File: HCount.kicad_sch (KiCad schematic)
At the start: 10 parts, among them U2 74HC11, U3 74HC163, U4 74HC163, U5 74HC163, U6 74HC688

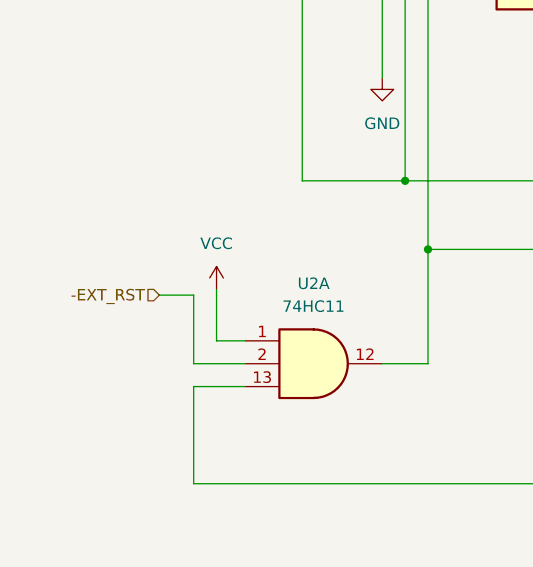
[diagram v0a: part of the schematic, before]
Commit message: allow hcount reset when frame ends
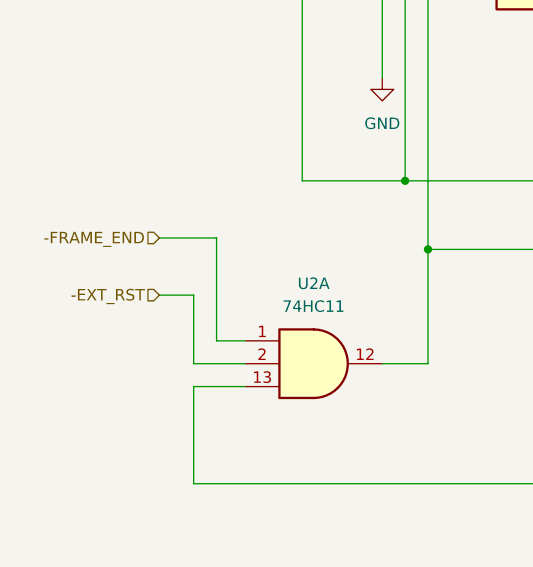
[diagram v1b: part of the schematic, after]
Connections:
- net VCC: no longer U2.1
- new net -FRAME_END: U2.1
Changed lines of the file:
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@@
+    (stroke (width 0) (type default))
+  )
+  (wire (pts (xy 27.305 126.365) (xy 33.655 126.365))
     (stroke (width 0) (type default))
   )
@@
     (stroke (width 0) (type default))
   )
-  (wire (pts (xy 33.655 132.08) (xy 33.655 137.795))
+  (wire (pts (xy 33.655 126.365) (xy 33.655 137.795))
     (stroke (width 0) (type default))
   )
@@
   (hierarchical_label "HC0" (shape output) (at 218.44 17.78 0) (fields_autoplaced)
     (effects (font (size 1.27 1.27)) (justify left))
+  )
+  (hierarchical_label "-FRAME_END" (shape input) (at 27.305 126.365 180) (fields_autoplaced)
+    (effects (font (size 1.27 1.27)) (justify right))
   )
   (hierarchical_label "HC1" (shape output) (at 218.44 20.32 0) (fields_autoplaced)
@@
         )
       )
-    )
-  )
-  (symbol (lib_id "power:VCC") (at 33.655 132.08 0) (unit 1)
-    (in_bom yes) (on_board yes) (dnp no) (fields_autoplaced)
-    (property "Reference" "#PWR03" (at 33.655 135.89 0)
-      (effects (font (size 1.27 1.27)) hide)
-    )
-    (property "Value" "VCC" (at 33.655 127 0)
-      (effects (font (size 1.27 1.27)))
-    )
-    (property "Footprint" "" (at 33.655 132.08 0)
-      (effects (font (size 1.27 1.27)) hide)
-    )
-    (property "Datasheet" "" (at 33.655 132.08 0)
-      (effects (font (size 1.27 1.27)) hide)
-    )
-    (pin "1")
-    (instances
-      (project "HW_VGA"
-        (path "/c4bd4b39-993a-4195-805f-b4de6fa4aea5/0f1cb3c4-c993-4160-bf3e-944843924f41"
-          (reference "#PWR03") (unit 1)
-        )
-      )

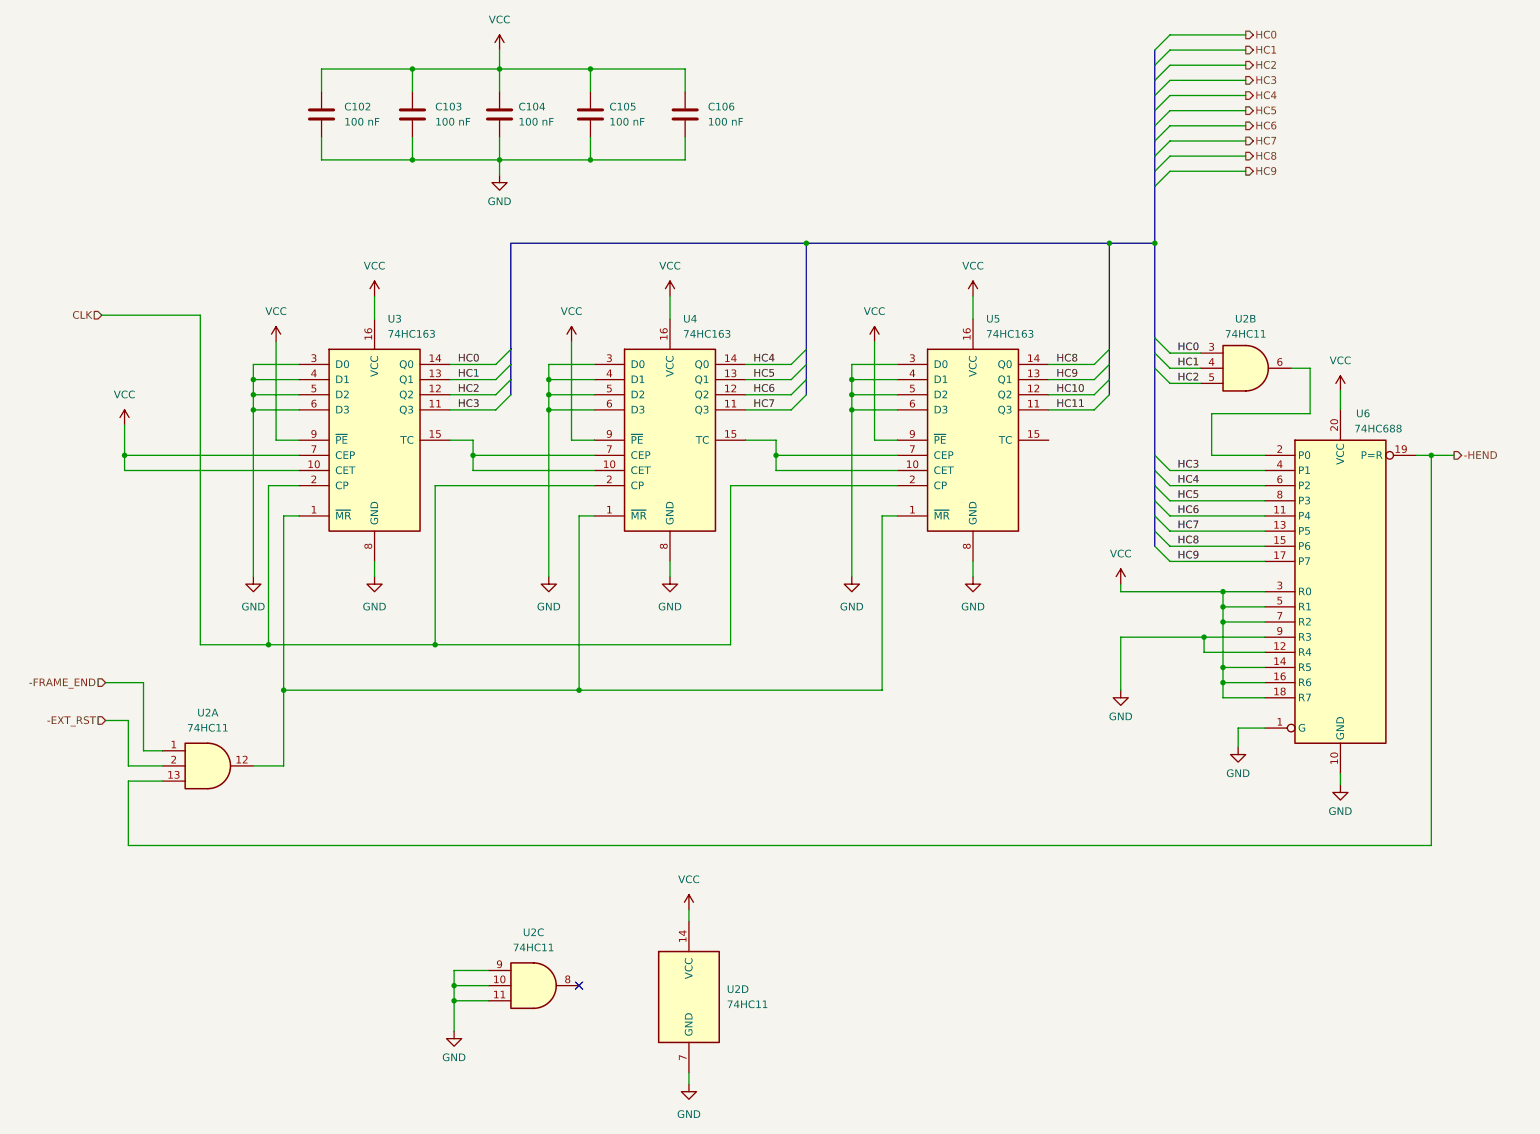
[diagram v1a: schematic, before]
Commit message: replace horizontal count logic with GAL22V10
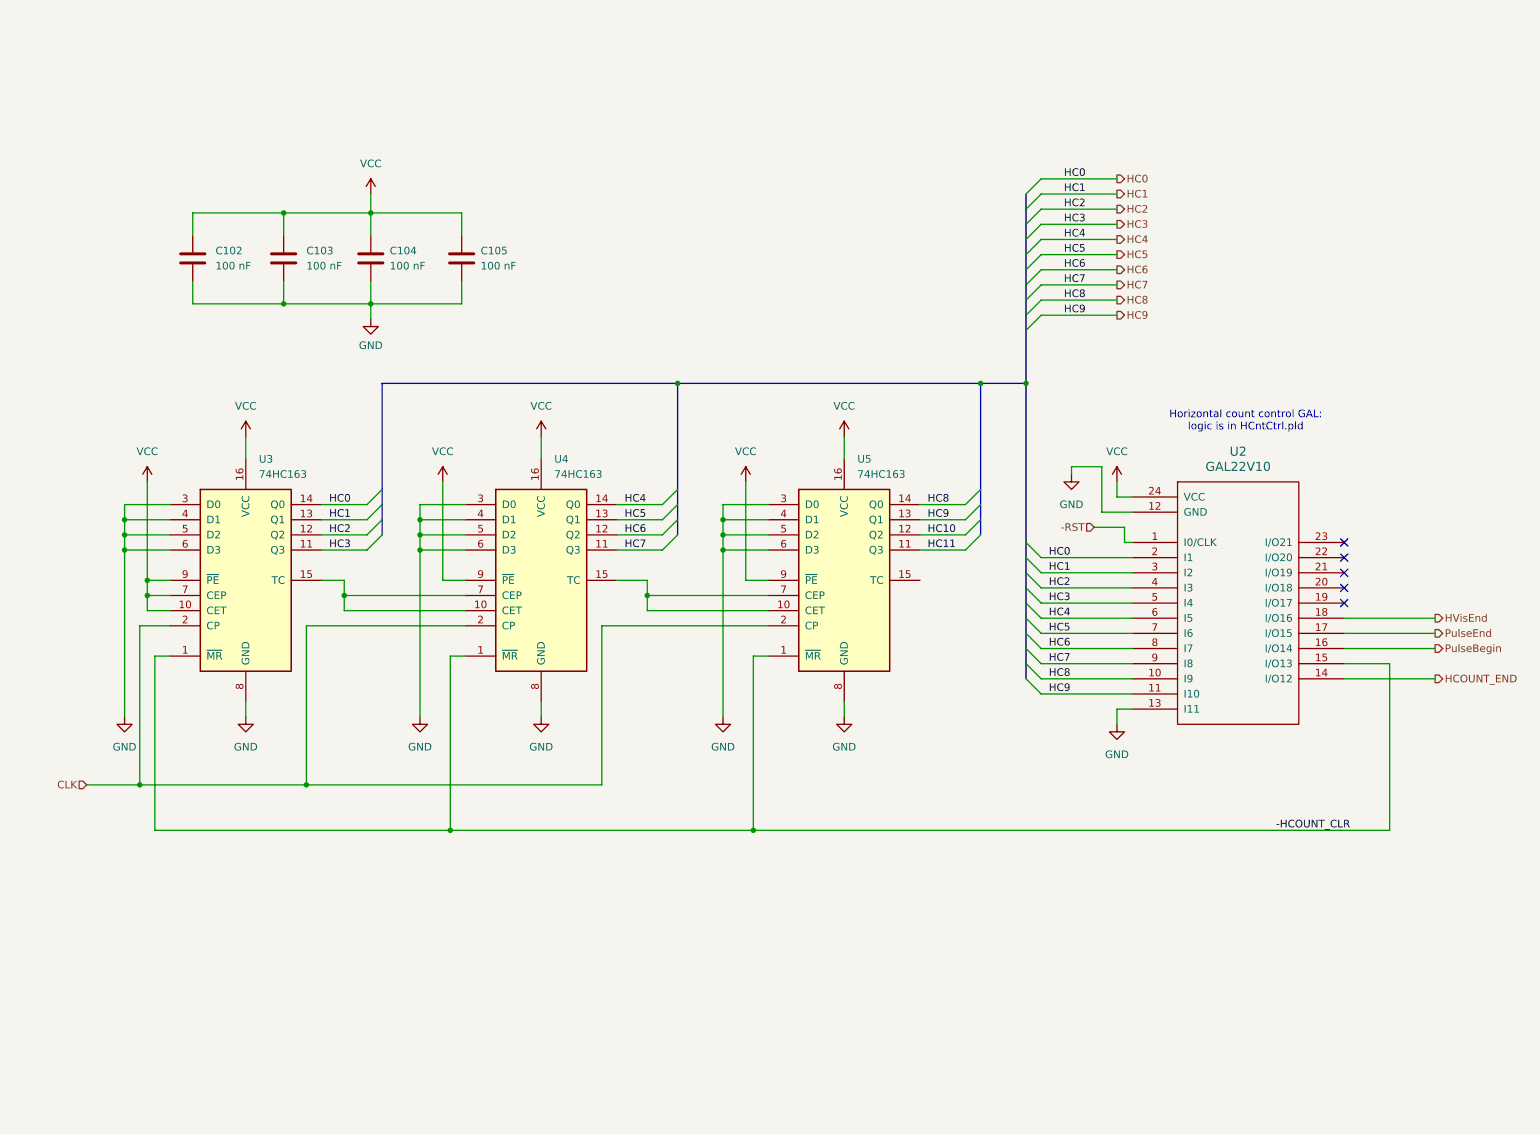
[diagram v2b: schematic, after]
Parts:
- removed C106: 100 nF, symbol Device:C
- removed U2: 74HC11, symbol 74xx:74LS11
- removed U6: 74HC688, symbol 74xx:74LS688
- added U2: GAL22V10, symbol ya68k:GAL22V10
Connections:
- net GND: now also U2.12 (GND), U2.13 (I11)
- net HC0: now also U2.2 (I1)
- net HC1: now also U2.3 (I2)
- net HC2: now also U2.4 (I3)
- net HC3: now also U2.5 (I4)
- net HC4: now also U2.6 (I5)
- net HC5: now also U2.7 (I6)
- net HC6: now also U2.8 (I7)
- net HC7: now also U2.9 (I8)
- net HC8: now also U2.10 (I9)
- net HC9: now also U2.11 (I10)
- net VCC: now also U2.24 (VCC)
- net -HCOUNT_CLR: now reaches U3.1 (~{MR}), U4.1 (~{MR}), U5.1 (~{MR})
- net -HCOUNT_CLR: now also U2.15 (I/O13)
- new net -RST: U2.1 (I0/CLK)
- new net HCOUNT_END: U2.14 (I/O12)
- new net HVisEnd: U2.18 (I/O16)
- new net PulseBegin: U2.16 (I/O14)
- new net PulseEnd: U2.17 (I/O15)
- no-connect marks 1 -> 5
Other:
- note added: "Horizontal count control GAL: logic is in HCntCtrl.pld"
- moved on the sheet: C102, C103, C104, C105, U3, U4, U5

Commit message: start working on VCount module
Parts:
- renumbered U2 to U102, U3 to U103, U4 to U104, U5 to U105
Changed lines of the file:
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@@
 		(dnp no)
 		(fields_autoplaced yes)
-		(property "Reference" "U3"
+		(property "Reference" "U103"
 			(at 52.9941 88.9 0)
 			(effects
@@
 			(project "HW_VGA"
 				(path "/c4bd4b39-993a-4195-805f-b4de6fa4aea5/0f1cb3c4-c993-4160-bf3e-944843924f41"
-					(reference "U3")
+					(reference "U103")
 					(unit 1)
 				)
@@
 		(dnp no)
 		(fields_autoplaced yes)
-		(property "Reference" "U2"
+		(property "Reference" "U102"
 			(at 217.17 87.63 0)
 			(effects
@@
 			(project "HW_VGA"
 				(path "/c4bd4b39-993a-4195-805f-b4de6fa4aea5/0f1cb3c4-c993-4160-bf3e-944843924f41"
-					(reference "U2")
+					(reference "U102")
 					(unit 1)
 				)
@@
 		(dnp no)
 		(fields_autoplaced yes)
-		(property "Reference" "U5"
+		(property "Reference" "U105"
 			(at 153.3241 88.9 0)
 			(effects
@@
 			(project "HW_VGA"
 				(path "/c4bd4b39-993a-4195-805f-b4de6fa4aea5/0f1cb3c4-c993-4160-bf3e-944843924f41"
-					(reference "U5")
+					(reference "U105")
 					(unit 1)
 				)
@@
 		(dnp no)
 		(fields_autoplaced yes)
-		(property "Reference" "U4"
+		(property "Reference" "U104"
 			(at 102.5241 88.9 0)
 			(effects
@@
 			(project "HW_VGA"
 				(path "/c4bd4b39-993a-4195-805f-b4de6fa4aea5/0f1cb3c4-c993-4160-bf3e-944843924f41"
-					(reference "U4")
-					(unit 1)
-				)
+					(reference "U104")
+					(unit 1)
+				)

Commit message: chips driven by GAL or memory need to be 74HCT
I forgot that GALs only guarantee 2.4V as the minimum
output high voltage. Bleh.
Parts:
- U103, U104, U105: value 74HC163 -> 74HCT163
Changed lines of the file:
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@@
 			)
 		)
-		(property "Value" "74HC163"
+		(property "Value" "74HCT163"
 			(at 52.9941 91.44 0)
 			(effects
@@
 			)
 		)
-		(property "Value" "74HC163"
+		(property "Value" "74HCT163"
 			(at 153.3241 91.44 0)
 			(effects
@@
 			)
 		)
-		(property "Value" "74HC163"
+		(property "Value" "74HCT163"
 			(at 102.5241 91.44 0)
 			(effects

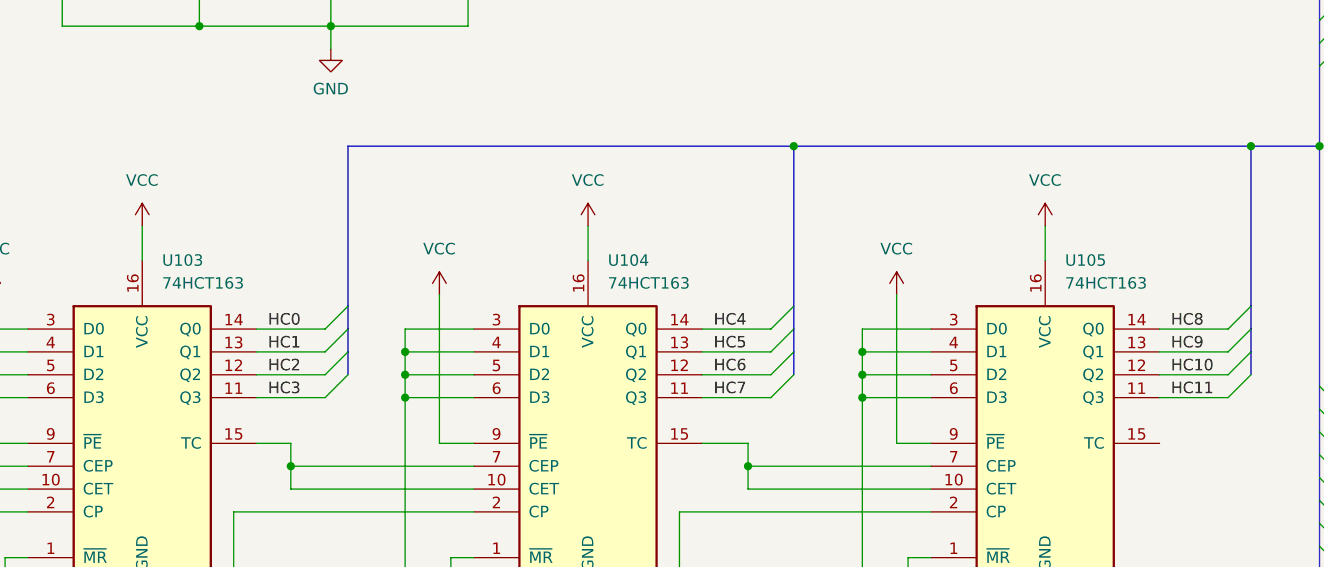
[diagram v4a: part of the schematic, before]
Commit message: use 74ACT parts where needed (e.g., HCount)
Also, I don't think the 74HCT365 buffer is needed for
the output DAC. I think a single intensity output can
feed into all three color outputs. It's a voltage source,
so it shouldn't really matter what load is on it.
(Need to test this out in simulation.)
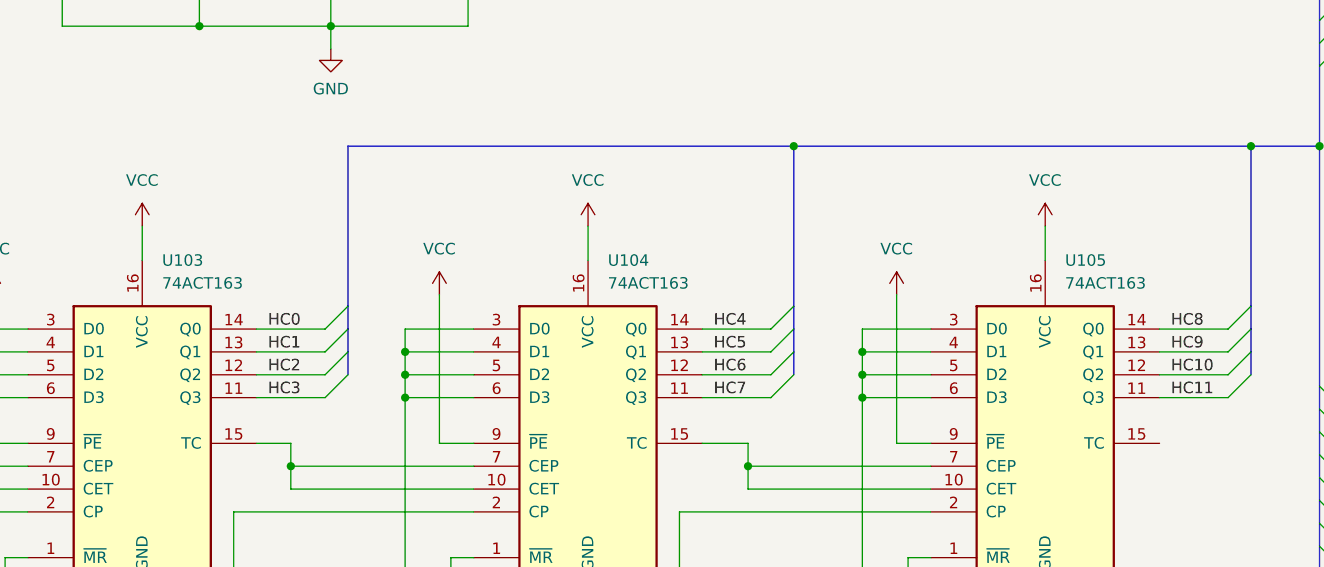
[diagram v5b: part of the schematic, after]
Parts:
- U103, U104, U105: value 74HCT163 -> 74ACT163
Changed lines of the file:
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@@
 			)
 		)
-		(property "Value" "74HCT163"
+		(property "Value" "74ACT163"
 			(at 52.9941 91.44 0)
 			(effects
@@
 			)
 		)
-		(property "Value" "74HCT163"
+		(property "Value" "74ACT163"
 			(at 153.3241 91.44 0)
 			(effects
@@
 			)
 		)
-		(property "Value" "74HCT163"
+		(property "Value" "74ACT163"
 			(at 102.5241 91.44 0)
 			(effects
